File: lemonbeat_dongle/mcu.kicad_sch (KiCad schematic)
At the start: 49 parts, among them J201 USB_A, J202 Prog, J203 u.FL, SW201 SW_Push, U201 nRF52840, Y201 32MHz, Y202 32.768kHz

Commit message: dongle: schematic & PCB: nRF52840 oscillator changes
- change footprint of capacitors for both crystals to 0402 so they can
  be exchanged more easily
- rotate Y201 for better symmetry
- no ground plane keepout area below crystals
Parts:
- C201, C202, C203, C204: footprint Capacitor_SMD:C_0201_0603Metric -> Capacitor_SMD:C_0402_1005Metric; Comment (none) -> Alternative at JLCPCB: C393682 / GCM1555C1H120FA16D; LCSC C384960 -> C161304; Part Number GRM0335C1H120FA01D -> GJM1555C1H120FB01D
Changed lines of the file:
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@@
     (property "Reference" "C204" (id 0) (at 151.13 57.15 90))
     (property "Value" "12pF" (id 1) (at 151.13 64.77 90))
-    (property "Footprint" "Capacitor_SMD:C_0201_0603Metric" (id 2) (at 154.94 59.9948 0)
+    (property "Footprint" "Capacitor_SMD:C_0402_1005Metric" (id 2) (at 154.94 59.9948 0)
       (effects (font (size 1.27 1.27)) hide)
     )
@@
       (effects (font (size 1.27 1.27)) hide)
     )
-    (property "Description" "50V 12pF C0G ±1% 0201" (id 4) (at 151.13 60.96 0)
-      (effects (font (size 1.27 1.27)) hide)
-    )
-    (property "LCSC" "C384960" (id 5) (at 151.13 60.96 0)
+    (property "Description" "50V 12pF C0G ±1% 0402" (id 4) (at 151.13 60.96 0)
+      (effects (font (size 1.27 1.27)) hide)
+    )
+    (property "LCSC" "C161304" (id 5) (at 151.13 60.96 0)
       (effects (font (size 1.27 1.27)) hide)
     )
@@
       (effects (font (size 1.27 1.27)) hide)
     )
-    (property "Part Number" "GRM0335C1H120FA01D" (id 7) (at 151.13 60.96 0)
+    (property "Part Number" "GJM1555C1H120FB01D" (id 7) (at 151.13 60.96 0)
+      (effects (font (size 1.27 1.27)) hide)
+    )
+    (property "Comment" "Alternative at JLCPCB: C393682 / GCM1555C1H120FA16D" (id 8) (at 151.13 60.96 0)
       (effects (font (size 1.27 1.27)) hide)
     )
@@
     (property "Reference" "C202" (id 0) (at 27.94 116.84 90))
     (property "Value" "12pF" (id 1) (at 27.94 119.38 90))
-    (property "Footprint" "Capacitor_SMD:C_0201_0603Metric" (id 2) (at 31.75 122.2248 0)
+    (property "Footprint" "Capacitor_SMD:C_0402_1005Metric" (id 2) (at 31.75 122.2248 0)
       (effects (font (size 1.27 1.27)) hide)
     )
@@
       (effects (font (size 1.27 1.27)) hide)
     )
-    (property "Description" "50V 12pF C0G ±1% 0201" (id 4) (at 27.94 123.19 0)
-      (effects (font (size 1.27 1.27)) hide)
-    )
-    (property "LCSC" "C384960" (id 5) (at 27.94 123.19 0)
+    (property "Description" "50V 12pF C0G ±1% 0402" (id 4) (at 27.94 123.19 0)
+      (effects (font (size 1.27 1.27)) hide)
+    )
+    (property "LCSC" "C161304" (id 5) (at 27.94 123.19 0)
       (effects (font (size 1.27 1.27)) hide)
     )
@@
       (effects (font (size 1.27 1.27)) hide)
     )
-    (property "Part Number" "GRM0335C1H120FA01D" (id 7) (at 27.94 123.19 0)
+    (property "Part Number" "GJM1555C1H120FB01D" (id 7) (at 27.94 123.19 0)
+      (effects (font (size 1.27 1.27)) hide)
+    )
+    (property "Comment" "Alternative at JLCPCB: C393682 / GCM1555C1H120FA16D" (id 8) (at 27.94 123.19 0)
       (effects (font (size 1.27 1.27)) hide)
     )
@@
     (property "Reference" "C203" (id 0) (at 151.13 46.99 90))
     (property "Value" "12pF" (id 1) (at 151.13 54.61 90))
-    (property "Footprint" "Capacitor_SMD:C_0201_0603Metric" (id 2) (at 147.32 51.7652 0)
+    (property "Footprint" "Capacitor_SMD:C_0402_1005Metric" (id 2) (at 147.32 51.7652 0)
       (effects (font (size 1.27 1.27)) hide)
     )
@@
       (effects (font (size 1.27 1.27)) hide)
     )
-    (property "Description" "50V 12pF C0G ±1% 0201" (id 4) (at 151.13 50.8 0)
-      (effects (font (size 1.27 1.27)) hide)
-    )
-    (property "LCSC" "C384960" (id 5) (at 151.13 50.8 0)
+    (property "Description" "50V 12pF C0G ±1% 0402" (id 4) (at 151.13 50.8 0)
+      (effects (font (size 1.27 1.27)) hide)
+    )
+    (property "LCSC" "C161304" (id 5) (at 151.13 50.8 0)
       (effects (font (size 1.27 1.27)) hide)
     )
@@
       (effects (font (size 1.27 1.27)) hide)
     )
-    (property "Part Number" "GRM0335C1H120FA01D" (id 7) (at 151.13 50.8 0)
+    (property "Part Number" "GJM1555C1H120FB01D" (id 7) (at 151.13 50.8 0)
+      (effects (font (size 1.27 1.27)) hide)
+    )
+    (property "Comment" "Alternative at JLCPCB: C393682 / GCM1555C1H120FA16D" (id 8) (at 151.13 50.8 0)
       (effects (font (size 1.27 1.27)) hide)
     )
@@
     (property "Reference" "C201" (id 0) (at 27.94 106.68 90))
     (property "Value" "12pF" (id 1) (at 27.94 109.22 90))
-    (property "Footprint" "Capacitor_SMD:C_0201_0603Metric" (id 2) (at 31.75 112.0648 0)
+    (property "Footprint" "Capacitor_SMD:C_0402_1005Metric" (id 2) (at 31.75 112.0648 0)
       (effects (font (size 1.27 1.27)) hide)
     )
@@
       (effects (font (size 1.27 1.27)) hide)
     )
-    (property "Description" "50V 12pF C0G ±1% 0201" (id 4) (at 27.94 113.03 0)
-      (effects (font (size 1.27 1.27)) hide)
-    )
-    (property "LCSC" "C384960" (id 5) (at 27.94 113.03 0)
+    (property "Description" "50V 12pF C0G ±1% 0402" (id 4) (at 27.94 113.03 0)
+      (effects (font (size 1.27 1.27)) hide)
+    )
+    (property "LCSC" "C161304" (id 5) (at 27.94 113.03 0)
       (effects (font (size 1.27 1.27)) hide)
     )
@@
       (effects (font (size 1.27 1.27)) hide)
     )
-    (property "Part Number" "GRM0335C1H120FA01D" (id 7) (at 27.94 113.03 0)
-      (effects (font (size 1.27 1.27)) hide)
-    )
+    (property "Part Number" "GJM1555C1H120FB01D" (id 7) (at 27.94 113.03 0)
+      (effects (font (size 1.27 1.27)) hide)
+    )
+    (property "Comment" "Alternative at JLCPCB: C393682 / GCM1555C1H120FA16D" (id 8) (at 27.94 113.03 0)
+      (effects (font (size 1.27 1.27)) hide)
+    )

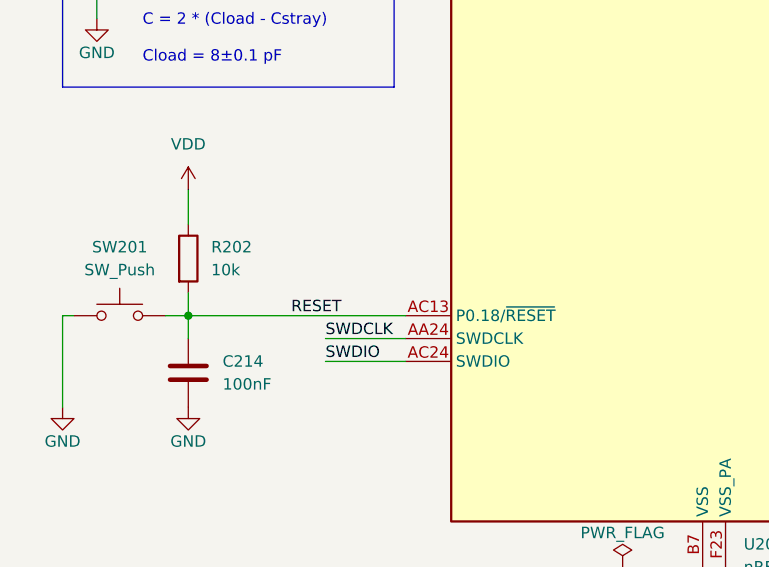
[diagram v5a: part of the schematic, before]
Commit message: dongle: add test point for SWDCLK & space test points further apart
This should allow creating a test jig even with test pads of 2mm
diameter.
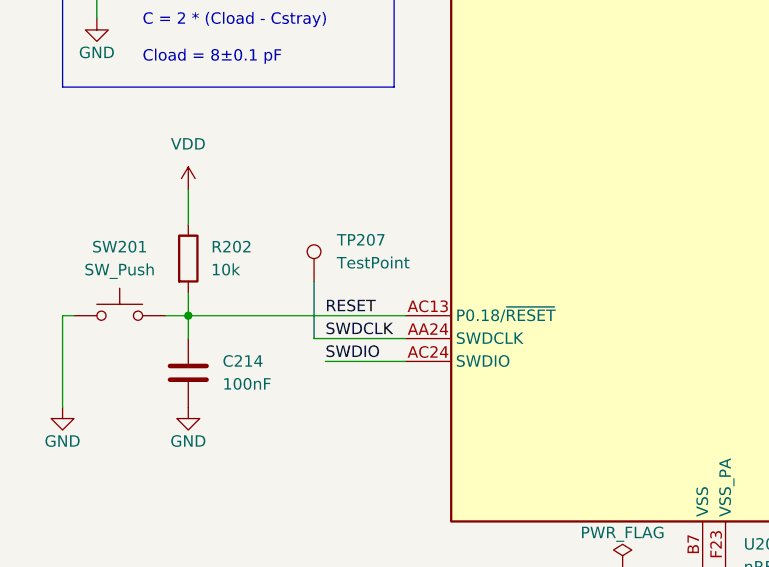
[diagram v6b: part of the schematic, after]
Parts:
- added TP207: TestPoint, TestPoint:TestPoint_Pad_D1.0mm, symbol Connector:TestPoint
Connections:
- net SWDCLK: now also TP207.1
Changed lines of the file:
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@@
     (stroke (width 0) (type default) (color 0 0 0 0))
   )
-  (wire (pts (xy 46.99 163.83) (xy 55.88 163.83))
+  (wire (pts (xy 45.72 163.83) (xy 55.88 163.83))
     (stroke (width 0) (type default) (color 0 0 0 0))
   )
@@
   )
   (wire (pts (xy 80.01 189.23) (xy 80.01 190.5))
+    (stroke (width 0) (type default) (color 0 0 0 0))
+  )
+  (wire (pts (xy 45.72 163.83) (xy 45.72 157.48))
     (stroke (width 0) (type default) (color 0 0 0 0))
   )
@@
     (effects (font (size 1.27 1.27)) (justify left bottom))
   )
-  (label "RESET" (at 43.18 161.29 0)
+  (label "RESET" (at 46.99 161.29 0)
     (effects (font (size 1.27 1.27)) (justify left bottom))
   )
@@
       (effects (font (size 1.27 1.27)) hide)
     )
+    (pin "1")
+  )
+  (symbol (lib_id "Connector:TestPoint") (at 45.72 157.48 0) (unit 1)
+    (in_bom yes) (on_board yes) (fields_autoplaced)
+    (property "Reference" "TP207" (id 0) (at 48.26 152.9079 0)
+      (effects (font (size 1.27 1.27)) (justify left))
+    )
+    (property "Value" "TestPoint" (id 1) (at 48.26 155.4479 0)
+      (effects (font (size 1.27 1.27)) (justify left))
+    )
+    (property "Footprint" "TestPoint:TestPoint_Pad_D1.0mm" (id 2) (at 50.8 157.48 0)
+      (effects (font (size 1.27 1.27)) hide)
+    )
+    (property "Datasheet" "~" (id 3) (at 50.8 157.48 0)
+      (effects (font (size 1.27 1.27)) hide)
+    )

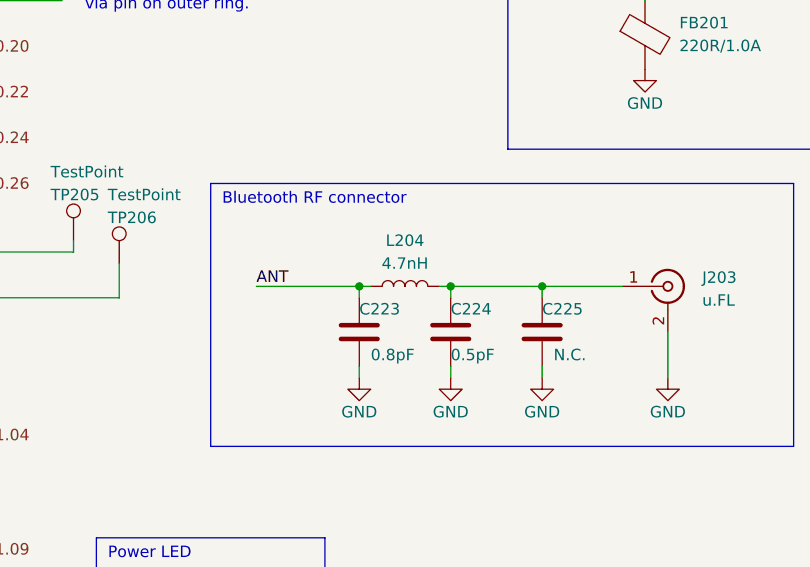
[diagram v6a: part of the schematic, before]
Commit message: dongle: update schematics & PCBs to KiCAD 7 & fix ERC/DRC errors & warnings
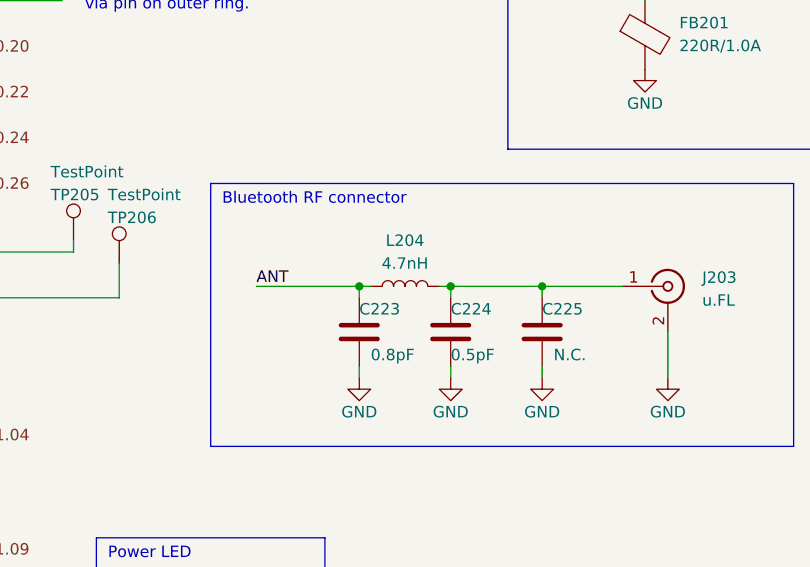
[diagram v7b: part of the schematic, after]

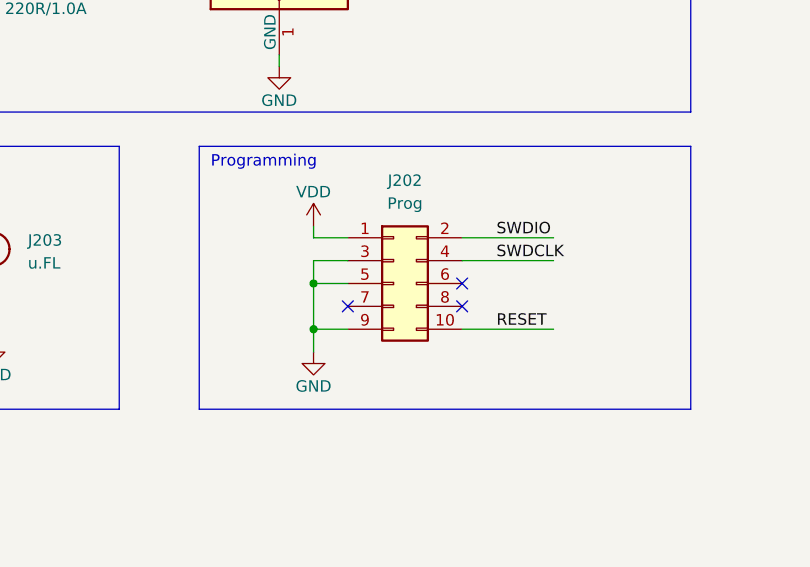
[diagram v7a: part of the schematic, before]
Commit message: dongle: add DNP for programming connector
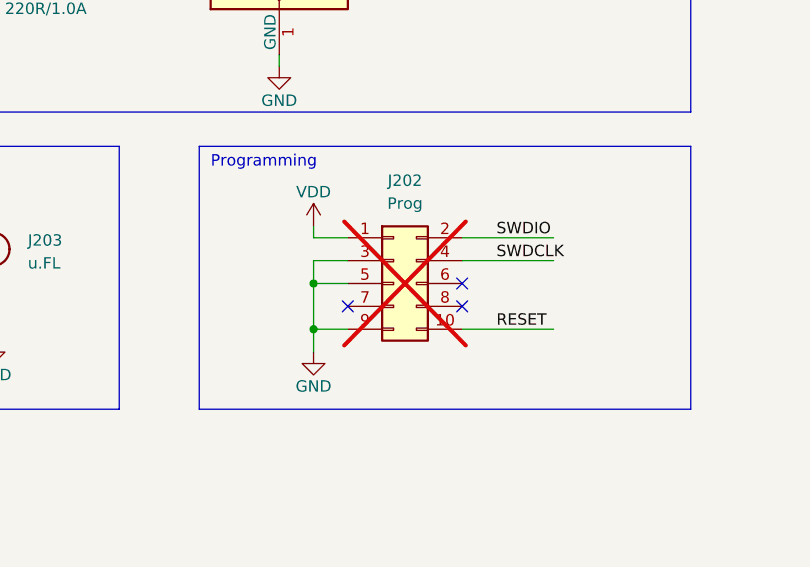
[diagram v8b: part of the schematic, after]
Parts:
- J202: now not fitted
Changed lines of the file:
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@@
   )
   (symbol (lib_id "Connector_Generic:Conn_02x05_Odd_Even") (at 246.38 133.35 0) (unit 1)
-    (in_bom yes) (on_board yes) (dnp no) (fields_autoplaced)
+    (in_bom yes) (on_board yes) (dnp yes) (fields_autoplaced)
     (property "Reference" "J202" (at 247.65 121.92 0)
       (effects (font (size 1.27 1.27)))
